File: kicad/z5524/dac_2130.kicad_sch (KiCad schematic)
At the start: 31 parts, among them U3 TL072, U4 AD5328

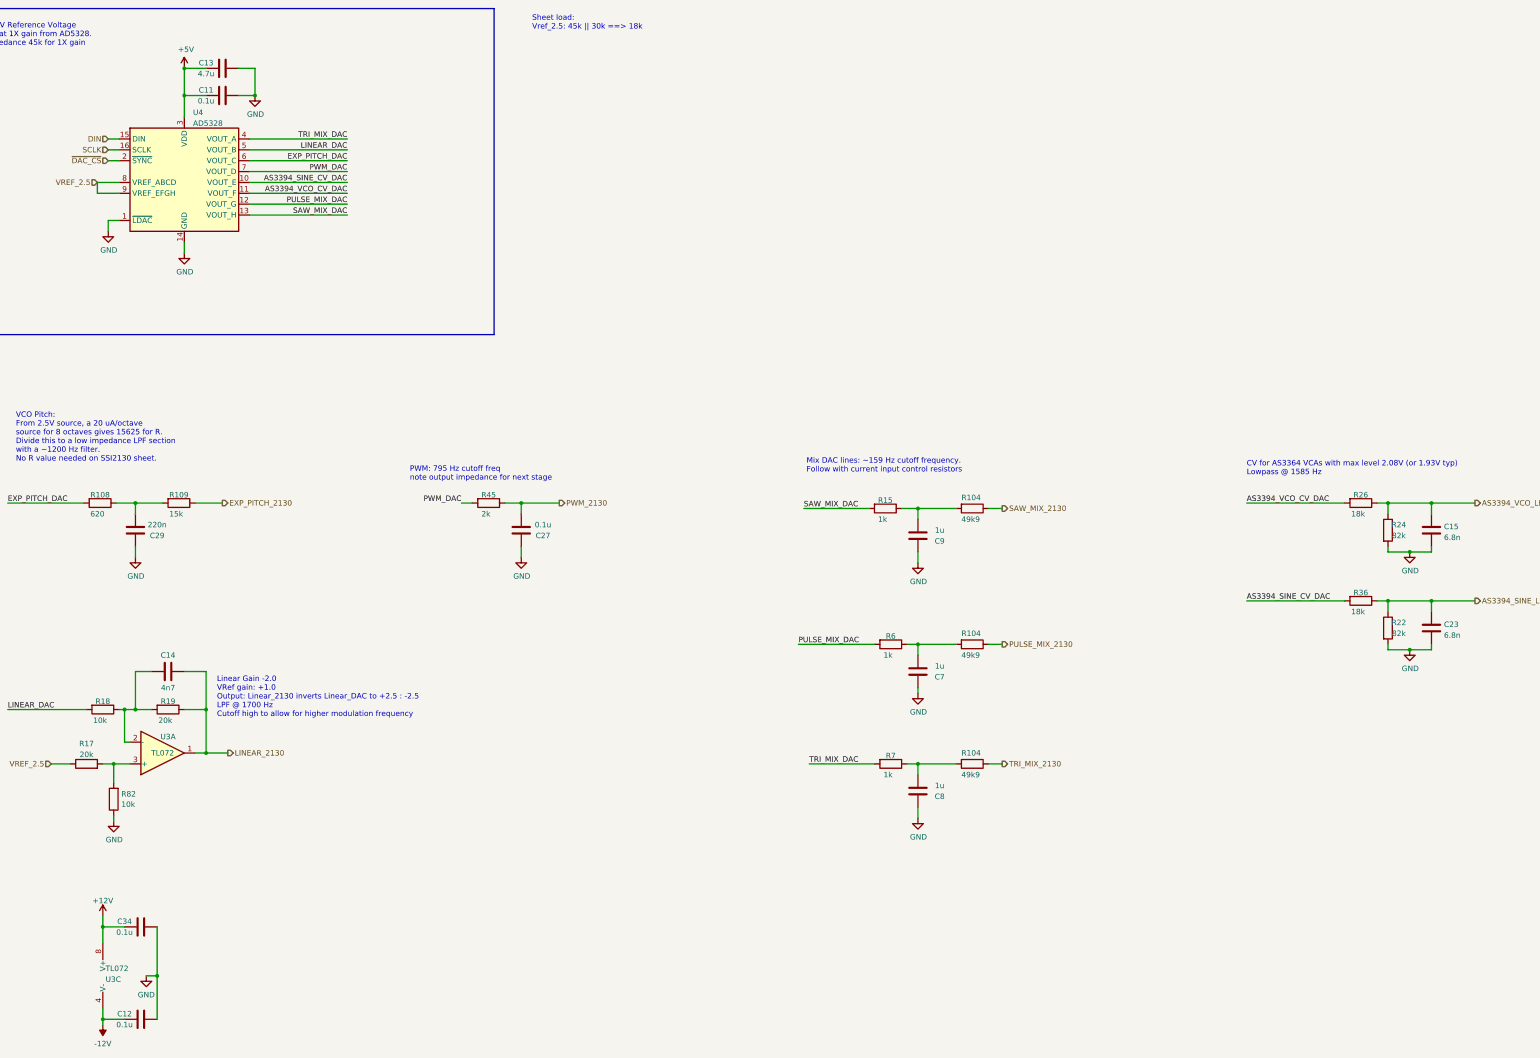
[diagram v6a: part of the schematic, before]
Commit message: getting silkscreen cleaned up
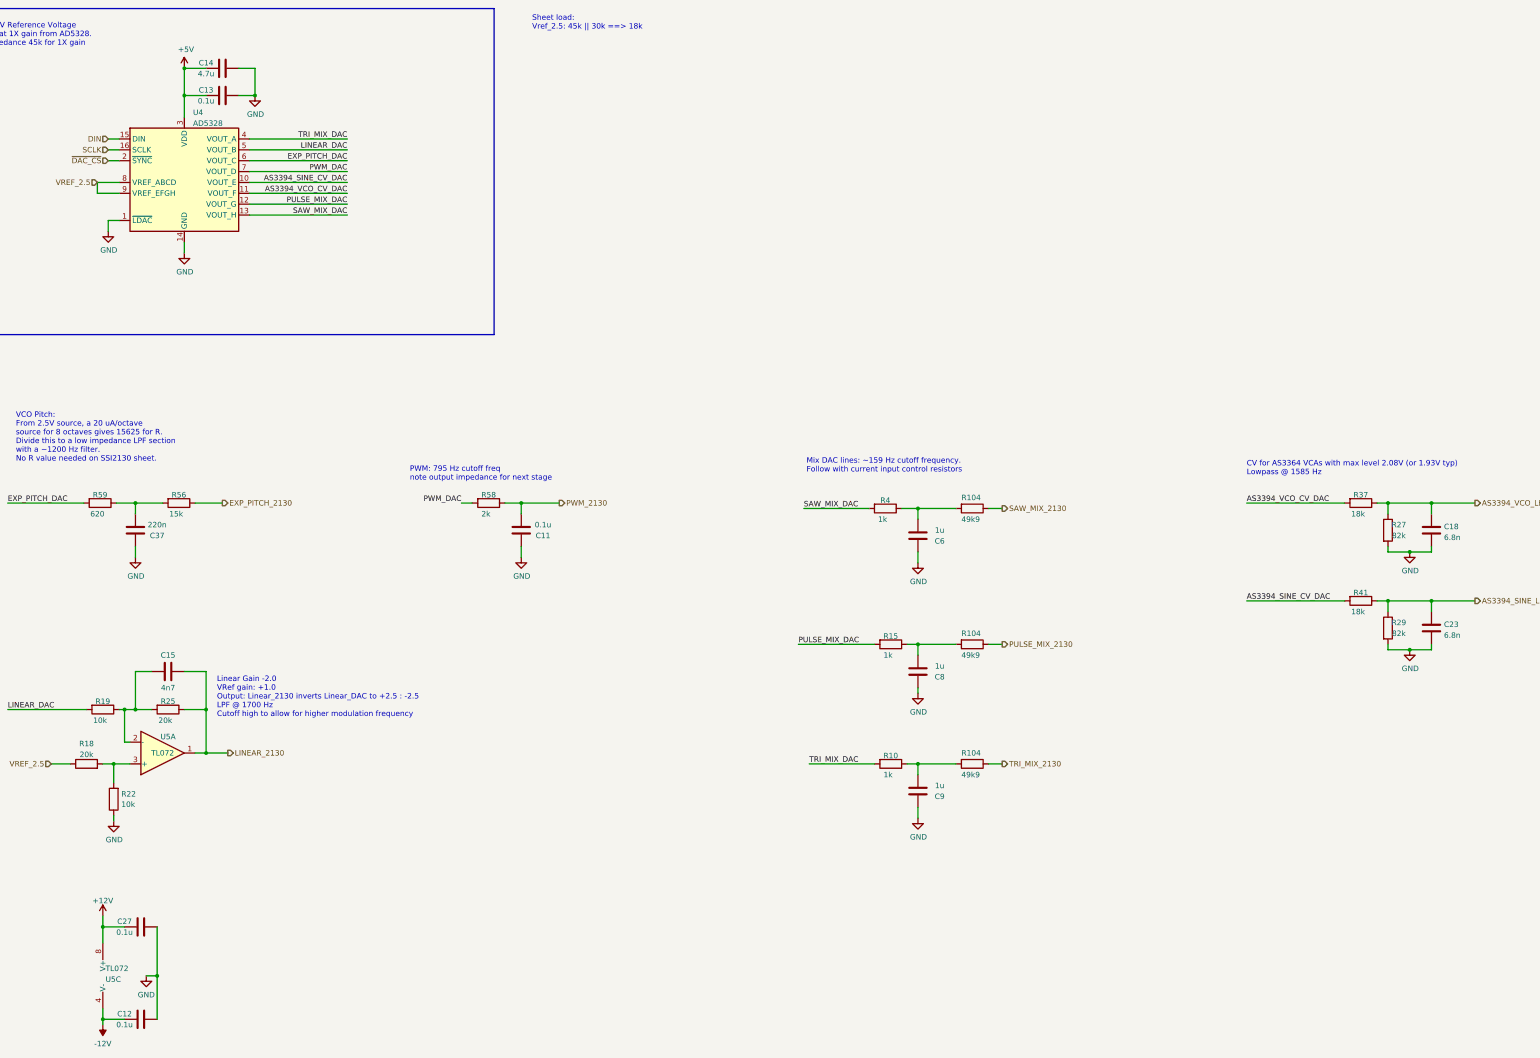
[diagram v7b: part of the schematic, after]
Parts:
- renumbered C27 to C11, C11 to C13, C13 to C14, C14 to C15, C15 to C18, C34 to C27, C29 to C37, C9 to C6, C7 to C8, C8 to C9, R7 to R10, R6 to R15, R17 to R18, R18 to R19, R82 to R22, R19 to R25, R24 to R27, R22 to R29, R26 to R37, R15 to R4, R36 to R41, R109 to R56, R45 to R58, R108 to R59, U3 to U5

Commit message: dist ref cap to two 1u instead of single; some more silkscreen cleanup
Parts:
- C11: LCSC (none) -> C14663
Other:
- moved on the sheet: C18, C23, R22, R27, R29, R37, R41, R59
